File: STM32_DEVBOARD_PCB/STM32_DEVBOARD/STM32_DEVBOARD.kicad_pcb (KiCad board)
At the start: 2 copper layers, 40 parts, among them J1 GT-USB-7002C, J2 Screw_Terminal_01x02, J3 SWD, Q1 AO3401A, U1 STM32F401RCTx, U2 USBLC6-2P6, U3 LIS2DW12, U4 TPMP2359DJ, U5 BME280

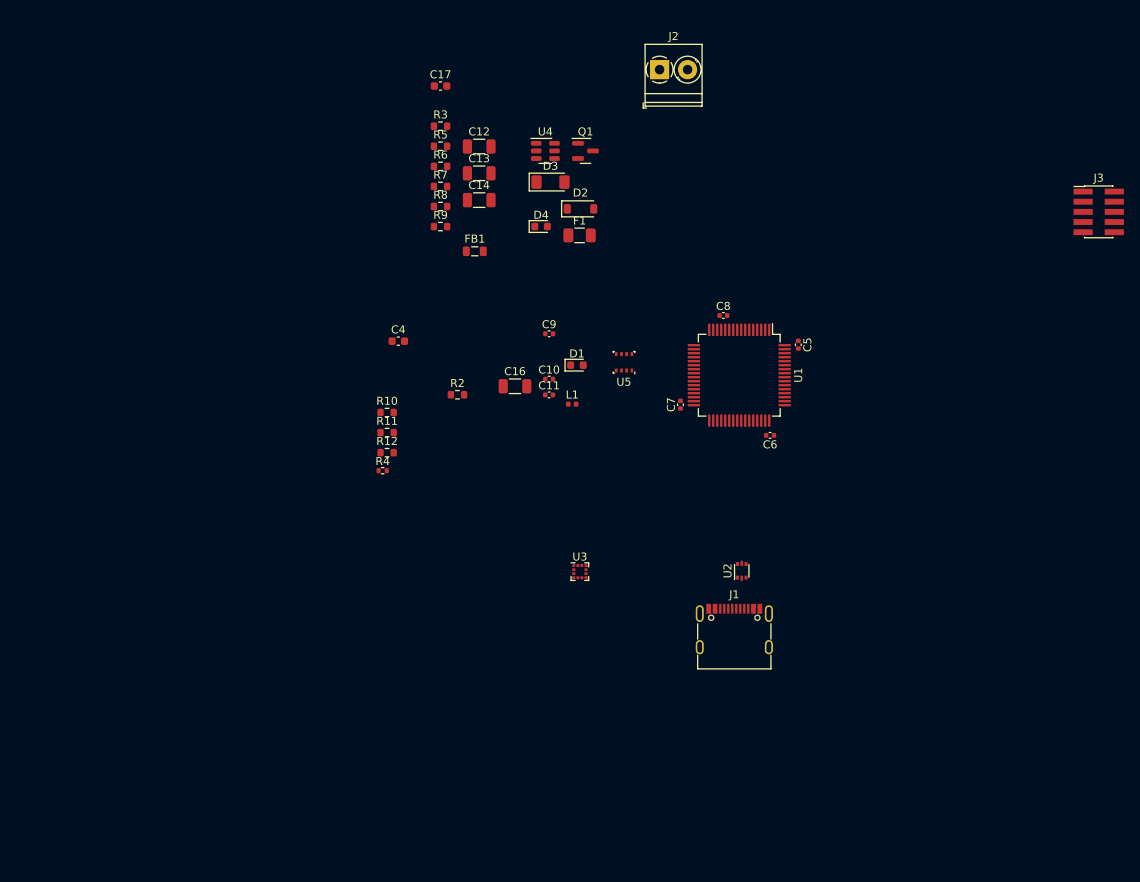
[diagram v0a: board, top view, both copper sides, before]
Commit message: Added USB C connector and tidy up traces.
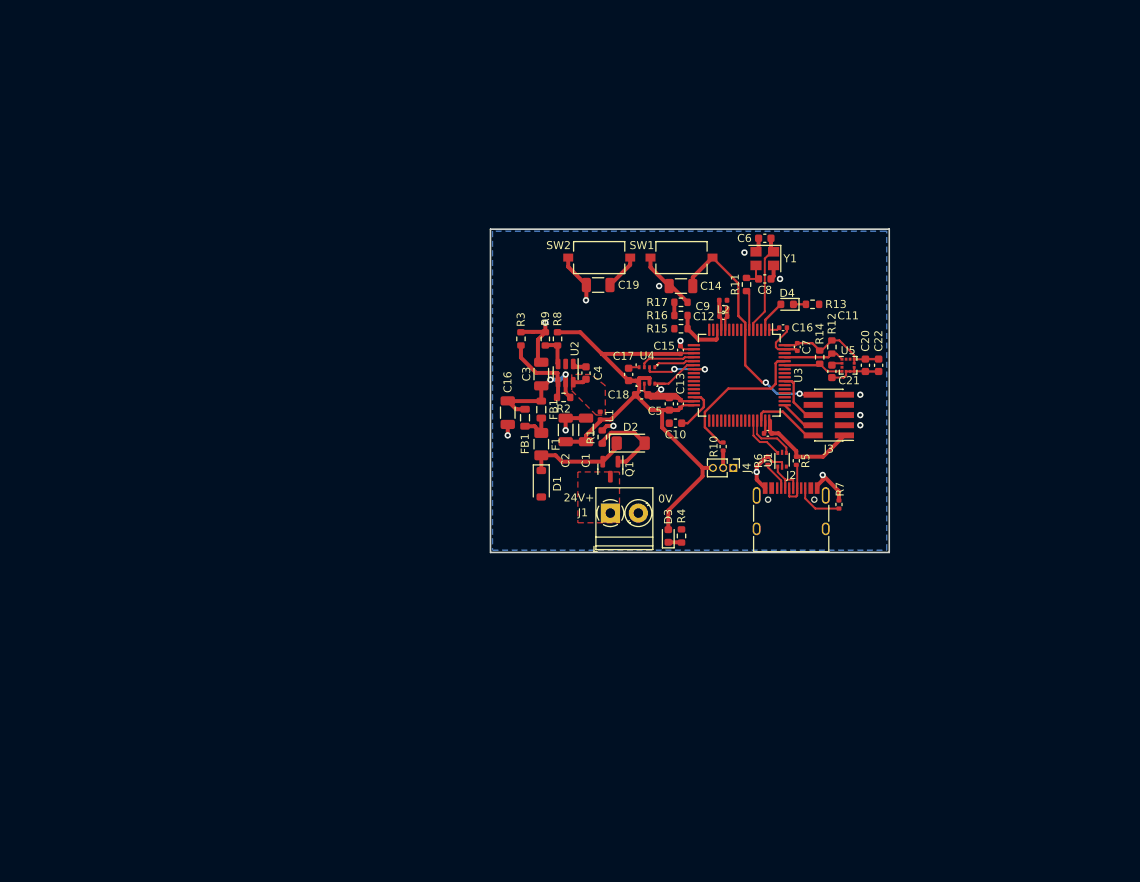
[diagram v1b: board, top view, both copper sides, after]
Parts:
- removed the J1 at (145.5, 127.0)
- added C10: 4u7, Capacitor_SMD:C_0603_1608Metric, F.Cu at (138.2, 100.1)
- added C14: 0u1, Capacitor_SMD:C_1206_3216Metric, F.Cu at (138.9, 82.9)
- added C17: 100n, Capacitor_SMD:C_0603_1608Metric, F.Cu at (132.3, 94.0)
- added C18: 100n, Capacitor_SMD:C_0603_1608Metric, F.Cu at (134.0, 96.5)
- added C19: 0u1, Capacitor_SMD:C_1206_3216Metric, F.Cu at (128.5, 82.8)
- added C20: 100n, Capacitor_SMD:C_0603_1608Metric, F.Cu at (161.9, 92.8)
- added C21: 100n, Capacitor_SMD:C_0603_1608Metric, F.Cu at (157.7, 93.6)
- added C22: 10u, Capacitor_SMD:C_0603_1608Metric, F.Cu at (163.6, 92.8)
- added C6: 10p, Capacitor_SMD:C_0603_1608Metric, F.Cu at (149.4, 77.0)
- added C8: 10p, Capacitor_SMD:C_0603_1608Metric, F.Cu at (149.4, 82.0)
- added FB1: 600 @ 600MHz, Inductor_SMD:L_0805_2012Metric, F.Cu at (119.4, 99.4)
- added J2: USB_C_Receptacle_USB2.0, Connector_USB:USB_C_Receptacle_HRO_TYPE-C-31-M-12, F.Cu at (152.7, 112.2)
- added J4: Conn_01x03_Pin, Connector_PinHeader_1.27mm:PinHeader_1x03_P1.27mm_Vertical, F.Cu at (145.4, 105.7)
- added L1: 4.7u, Inductor_SMD:L_0402_1005Metric, F.Cu at (128.8, 99.1)
- added R11: R47, Resistor_SMD:R_0603_1608Metric, F.Cu at (147.1, 82.7)
- added R12: 10k, Resistor_SMD:R_0603_1608Metric, F.Cu at (157.7, 90.6)
- added R14: 10k, Resistor_SMD:R_0603_1608Metric, F.Cu at (156.2, 91.8)
- added R5: 1k5, Resistor_SMD:R_0402_1005Metric, F.Cu at (153.3, 104.8)
- added R6: 5k1, Resistor_SMD:R_0402_1005Metric, F.Cu at (149.7, 104.8)
- added R7: 5k1, Resistor_SMD:R_0402_1005Metric, F.Cu at (158.6, 110.2)
- added SW1: BTN_RSET, Button_Switch_SMD:SW_Tactile_SPST_NO_Straight_CK_PTS636Sx25SMTRLFS, F.Cu at (138.9, 79.4)
- added SW2: BTN1, Button_Switch_SMD:SW_Tactile_SPST_NO_Straight_CK_PTS636Sx25SMTRLFS, F.Cu at (128.7, 79.4)
- added Y1: 16MHz, Crystal:Crystal_SMD_3225-4Pin_3.2x2.5mm, F.Cu at (149.4, 79.5)
- moved J1 55.8 mm to (130.0, 111.3)
- moved R4 51.0 mm to (138.9, 114.2), turned to -90 degrees
- moved R13 45.8 mm to (155.3, 85.2), turned to 180 degrees
- moved R1 43.8 mm to (129.0, 101.8), turned to 90 degrees
- moved R10 42.7 mm to (144.1, 103.0), turned to 90 degrees
- moved U5 42.3 mm to (159.8, 92.8)
- moved J3 42.2 mm to (157.4, 99.1), turned to 180 degrees
- moved D3 41.8 mm to (137.3, 114.2), turned to 90 degrees
- moved R17 41.3 mm to (138.9, 85.0), turned to 180 degrees
- moved C4 40.2 mm to (127.0, 93.8), turned to 90 degrees
- moved Q1 39.9 mm to (130.0, 105.8), turned to -90 degrees
- moved R15 39.0 mm to (138.9, 88.3), turned to 180 degrees
- moved R16 38.7 mm to (138.9, 86.6)
- moved C5 34.8 mm to (137.4, 97.7), turned to 90 degrees
- moved C1 34.7 mm to (127.0, 100.9), turned to 90 degrees
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- renumbered C13 to C1, C6 to C11, C11 to C12, C7 to C13, C8 to C15, C9 to C16, C14 to C2, C12 to C3, C17 to C4, C4 to C5, C5 to C7, C10 to C9, D2 to D1, D3 to D2, D4 to D3, D1 to D4, J2 to J1, L1 to L2, R3 to R1, R4 to R10, R2 to R13, R11 to R15, R10 to R16, R12 to R17, R7 to R2, R9 to R3, R8 to R4, R5 to R8, R6 to R9, U2 to U1, U4 to U2, U1 to U3, U5 to U4, U3 to U5
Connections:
- net USB_OTG_FS_DM_- renamed USB_OTG_FS_DN
- net USB_OTG_FS_DP_+ renamed USB_OTG_FS_DP
- C1 pad 1: +3V3 -> +3.3V
- C11 pad 1: +3V3 -> +3.3V
- C13 pad 1: +3V3 -> +3.3V
- C15 pad 1: +3V3 -> +3.3V
- C16 pad 1: +3V3 -> +3.3V
- C2 pad 1: +3V3 -> +3.3V
- C5 pad 1: +3V3 -> +3.3V
- C7 pad 1: +3V3 -> +3.3V
- D3 pad 2: +3V3 -> +3.3V
- J3 pad 1: +3V3 -> +3.3V
- L2 pad 1: +3V3 -> +3.3V
- R8 pad 1: +3V3 -> +3.3V
- U3 pad 20: unconnected-(U1-PA4-Pad20) -> SPI1_CSB
- U3 pad 41: SPI1_CSB -> unconnected-(U3-PA8-Pad41)
- U5 pad 10: +3V3 -> +3.3V
- U5 pad 2: +3V3 -> +3.3V
- U5 pad 9: +3V3 -> +3.3V
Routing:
- net +3.3V: track 0.00 -> 102.8 mm
- net GND: track 0.00 -> 81.9 mm, vias 0 -> 9
- net NRST: track 0.00 -> 29.8 mm, vias 0 -> 2
- net BOOT0: track 0.00 -> 19.1 mm
- net BUCK_IN: track 0.00 -> 15.6 mm, vias 0 -> 2
- net Net-(D1-K): track 0.00 -> 13.0 mm
- net RCC_OSC_IN: track 0.00 -> 12.8 mm
- net Net-(D2-A): track 0.00 -> 11.0 mm
- net BUCK_EN: track 0.00 -> 10.1 mm
- net SPI1_MOSI: track 0.00 -> 8.98 mm, vias 0 -> 2
- net SWDIO: track 0.00 -> 8.70 mm
- net I2C1_SCL: track 0.00 -> 7.65 mm
- net I2C1_SDA: track 0.00 -> 7.64 mm
- net SPI1_MISO: track 0.00 -> 7.11 mm
- net VMEAS: track 0.00 -> 7.08 mm
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- added copper zone on F.Cu, net +24V
- added copper zone on F.Cu, net BUCK_SW
- added copper zone on B.Cu, net GND
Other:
- board outline added: 49.8 x 40.4 mm
- board text added: "0V"
- board text added: "24V+"

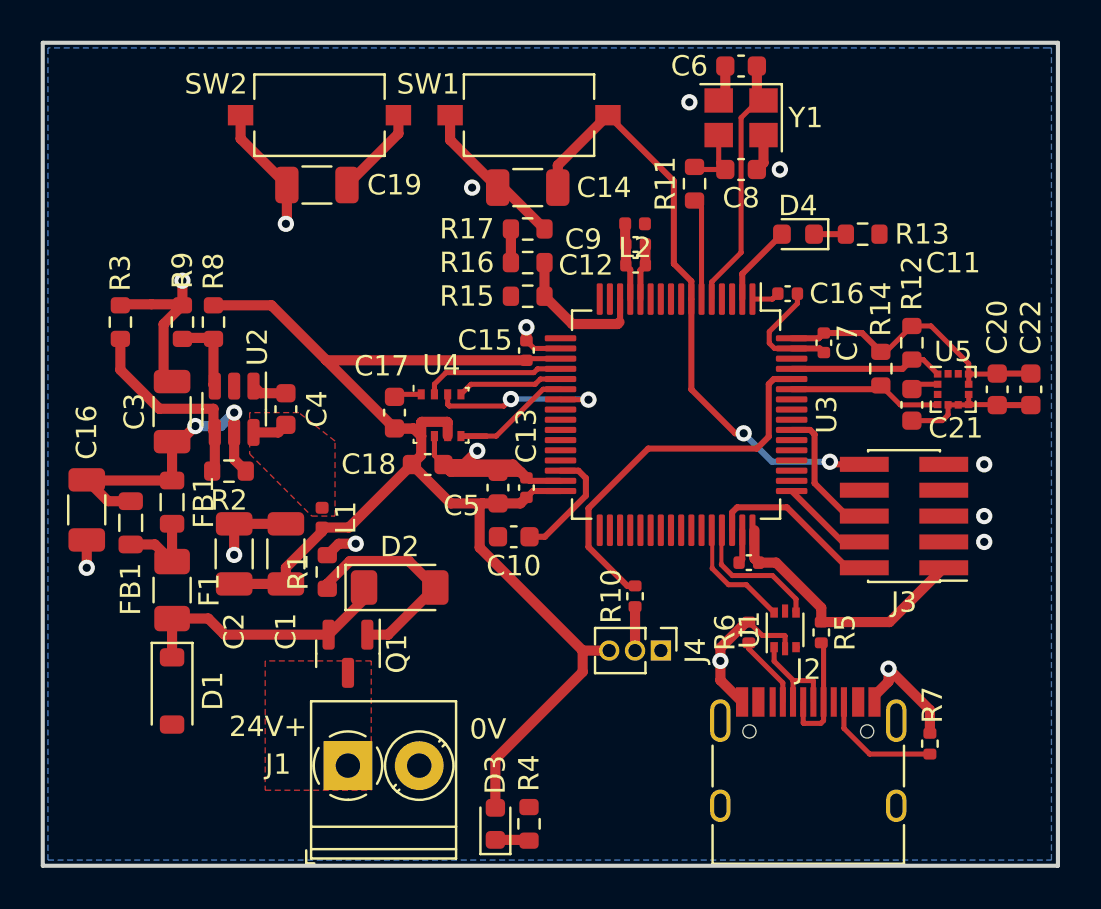
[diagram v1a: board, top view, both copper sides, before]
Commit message: Added images and more tidy of PCB
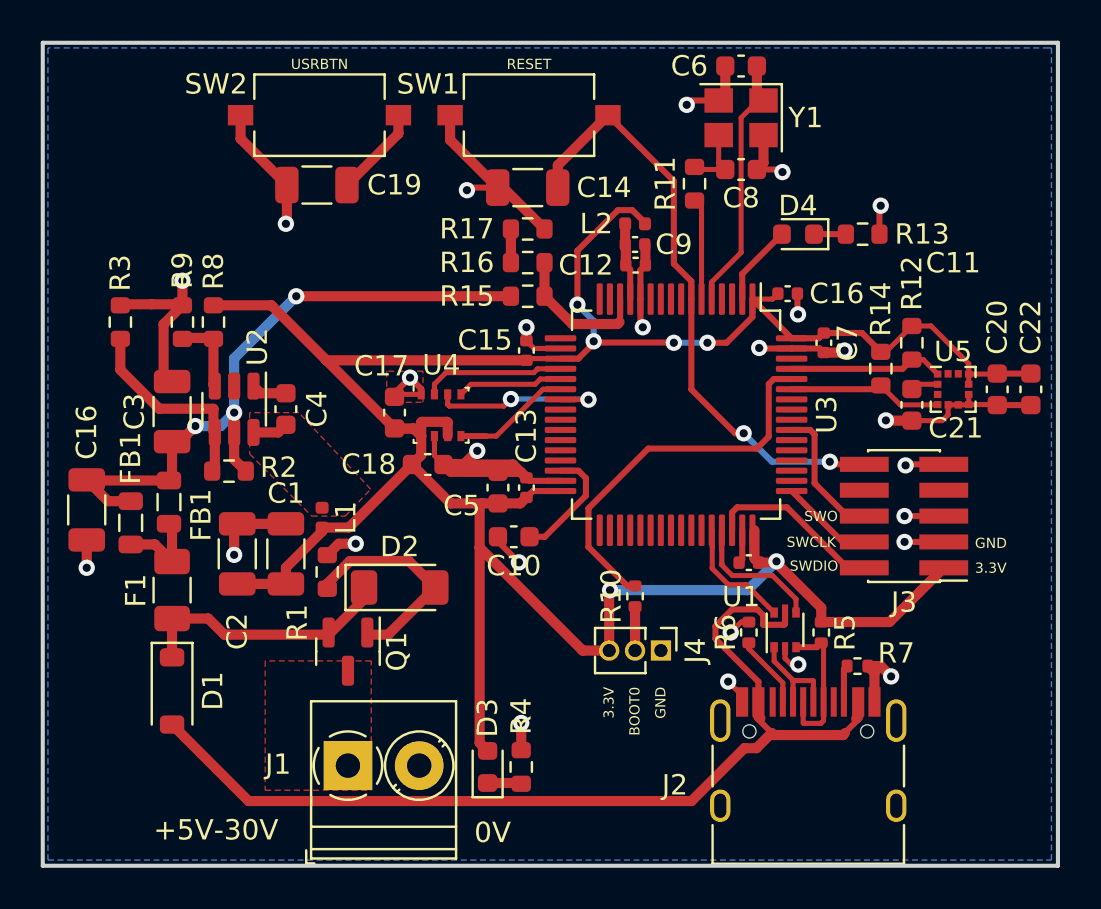
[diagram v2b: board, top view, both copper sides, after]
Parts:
- moved R7 5.21 mm to (155.1, 106.4), turned to 0 degrees
- moved D3 2.82 mm to (136.9, 111.4)
- moved R4 2.82 mm to (138.6, 111.4)
- moved C2 0.15 mm to (124.6, 100.9)
- moved FB1 0.15 mm to (121.3, 98.4)
- moved Q1 0.11 mm to (130.0, 105.7)
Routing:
- net +5V: track 0.00 -> 50.9 mm
- net +3.3V: track 102.8 -> 138.4 mm, vias 0 -> 6
- net BUCK_IN: track 15.6 -> 33.1 mm, vias 2 -> 3
- net GND: track 81.9 -> 94.3 mm, vias 9 -> 26
- net USB_CONN_CC2: track 6.04 -> 1.83 mm
- net USB_OTG_FS_DP: track 6.85 -> 8.52 mm
- net USB_CONN_D+: track 6.04 -> 7.37 mm
- net (no net): vias 6 -> 0
- added copper zone on F.Cu, net GND
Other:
- board text added: "+5V-30V"
- board text added: "3.3V"
- board text added: "BOOT0"
- board text added: "GND"
- board text added: "RESET"
- board text added: "SWCLK"
- board text added: "SWDIO"
- board text added: "SWO"
- board text added: "USRBTN"
- board text removed: "24V+"

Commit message: Added images of render
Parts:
- removed the C16 at (117.2, 98.8)
- removed the FB1 at (121.3, 98.4)
- added H1: MountingHole, MountingHole:MountingHole_4.3mm_M4_Pad, F.Cu at (86.8, 147.1)
- added H2: MountingHole, MountingHole:MountingHole_4.3mm_M4_Pad, F.Cu at (86.8, 57.0)
- moved C11 54.7 mm to (96.0, 91.1)
- moved C12 54.7 mm to (90.5, 76.5)
- moved C13 54.7 mm to (85.1, 87.4)
- moved C14 54.7 mm to (85.2, 72.7)
- moved C15 54.7 mm to (85.1, 80.7)
- moved C16 54.7 mm to (97.9, 77.9)
- moved C17 54.7 mm to (78.6, 83.7)
- moved C19 54.7 mm to (74.8, 72.5)
- moved C20 54.7 mm to (108.2, 82.6)
- moved C22 54.7 mm to (109.9, 82.6)
- moved C3 54.7 mm to (67.7, 83.7)
- moved C6 54.7 mm to (95.6, 66.7)
- moved C8 54.7 mm to (95.6, 71.8)
- moved C9 54.7 mm to (90.4, 75.5)
- moved D1 54.7 mm to (67.7, 97.4)
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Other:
- board size 49.8 x 40.4 mm -> 49.8 x 103.9 mm
- board text added: "CLK"
- board text added: "IO"
- board text added: "O"
- board text added: "RST"
- board text removed: "SWCLK"
- board text removed: "SWDIO"
- board text removed: "SWO"

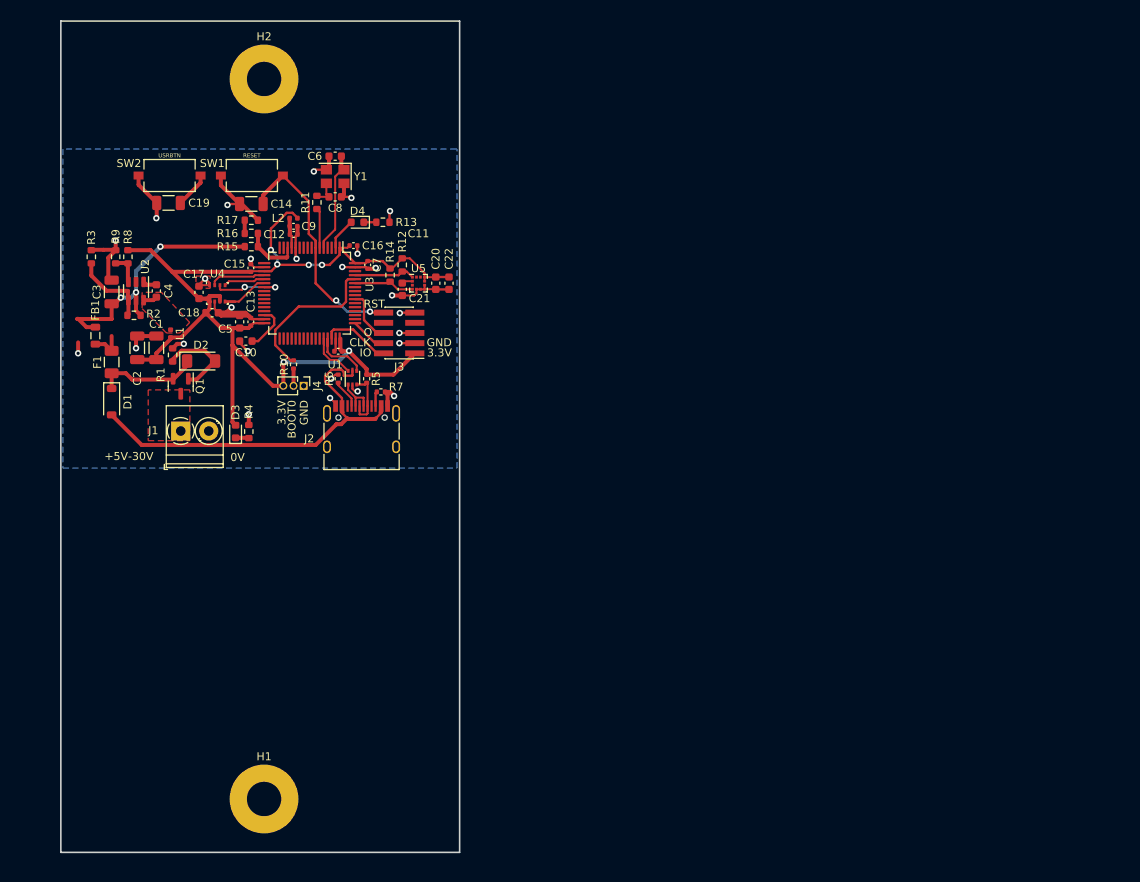
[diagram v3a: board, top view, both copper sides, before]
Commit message: Upgrade picture quality
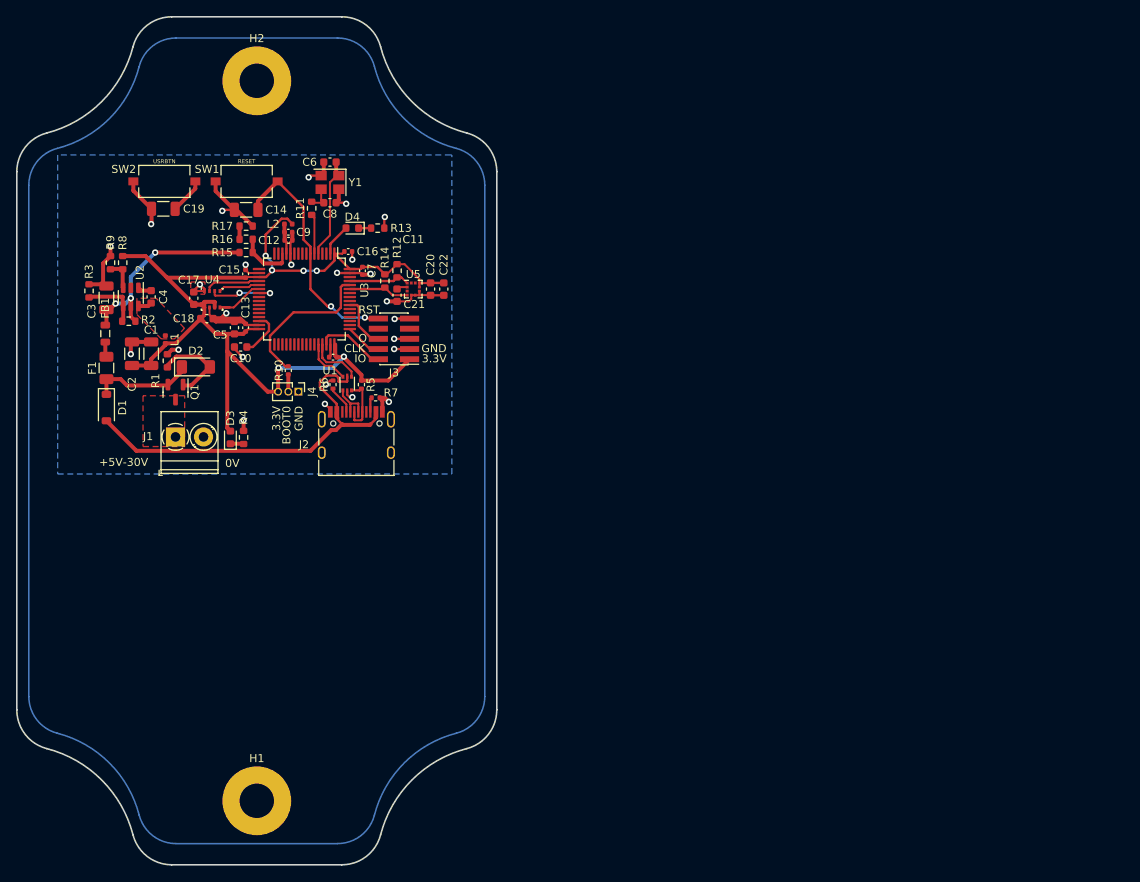
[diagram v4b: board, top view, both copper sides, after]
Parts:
- moved R3 4.27 mm to (64.9, 83.5)
- moved FB1 1.26 mm to (66.9, 88.9)
- moved U3 0.98 mm to (91.8, 84.6)
- moved C1 0.98 mm to (72.6, 91.4)
- moved C10 0.98 mm to (83.8, 90.6)
- moved C11 0.98 mm to (95.4, 91.8)
- moved C12 0.98 mm to (89.8, 77.2)
- moved C13 0.98 mm to (84.5, 88.1)
- moved C14 0.98 mm to (84.5, 73.4)
- moved C15 0.98 mm to (84.5, 81.4)
- moved C16 0.98 mm to (97.3, 78.6)
- moved C17 0.98 mm to (78.0, 84.5)
- moved C18 0.98 mm to (79.6, 87.0)
- moved C2 0.98 mm to (70.3, 91.4)
- moved C20 0.98 mm to (107.6, 83.3)
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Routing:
- net BUCK_IN: track 33.1 -> 26.3 mm
- net BUCK_EN: track 10.1 -> 7.39 mm
- net Net-(F1-Pad1): track 4.24 -> 1.89 mm
- net GND: track 94.3 -> 92.2 mm, vias 26 -> 25
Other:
- board size 49.8 x 103.9 mm -> 60 x 106 mm

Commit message: Updates to board and start to populate BOM
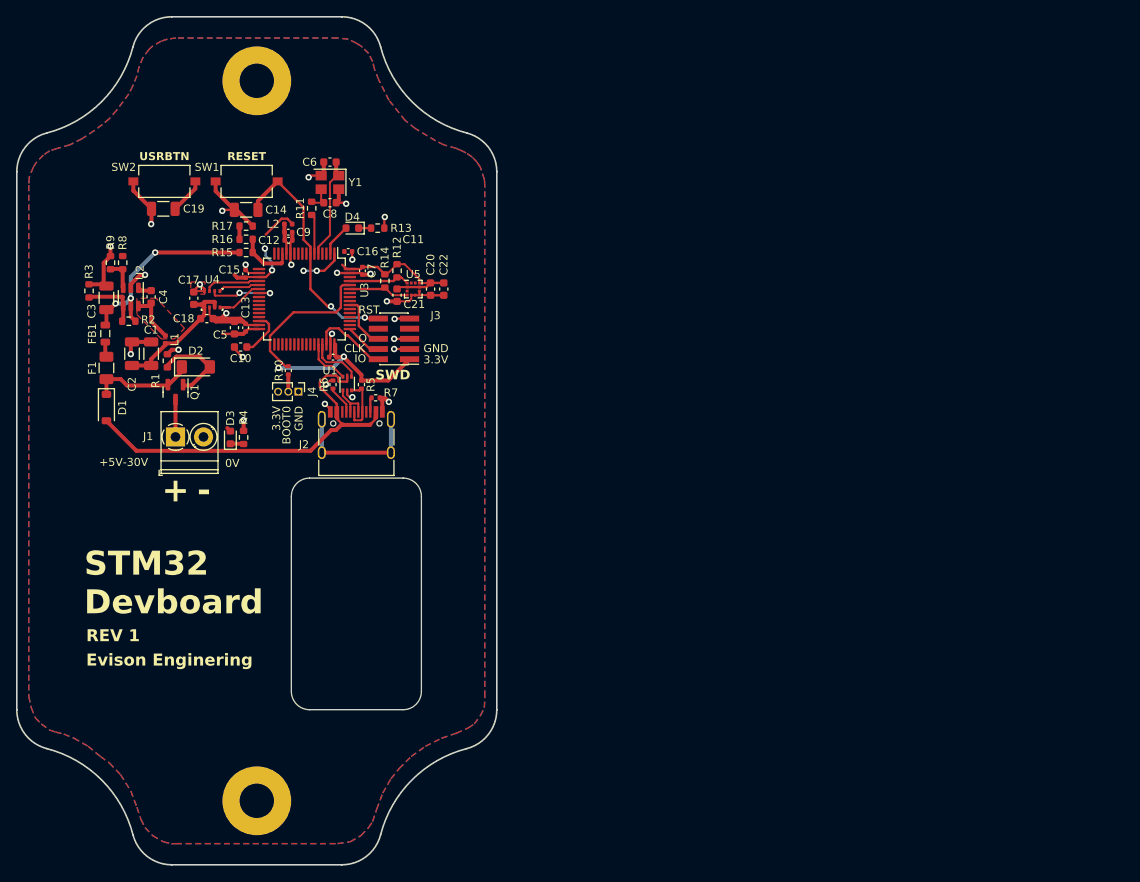
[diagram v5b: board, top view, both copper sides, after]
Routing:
- net +3.3V: track 138.4 -> 86.1 mm
- net unconnected-(J2-SHIELD-PadS1): track 0.00 -> 17.0 mm
- net BUCK_SW: track 1.74 -> 6.56 mm
- net +24V: track 0.00 -> 4.66 mm
- net GND: track 92.2 -> 96.9 mm, vias 25 -> 27
- net SWDIO: track 8.70 -> 9.85 mm
- added copper zone on F.Cu, net +3.3V
- removed copper zone on F.Cu, net +24V
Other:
- outline, holes or cut-outs redrawn
- board text added: "+"
- board text added: "-"
- board text added: "Evison Enginering"
- board text added: "REV 1"
- board text added: "STM32 Devboard"
- board text added: "SWD"
